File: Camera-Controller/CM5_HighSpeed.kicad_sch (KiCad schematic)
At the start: 19 parts, among them J10 690-019-298-412, J12 USB3_A, J16 Conn_01x22_Female, J22 690-019-298-412, J5 Conn_01x22_Female, J6 THD-02-R, U12 RT9742SNGV, U6 AP22653W6

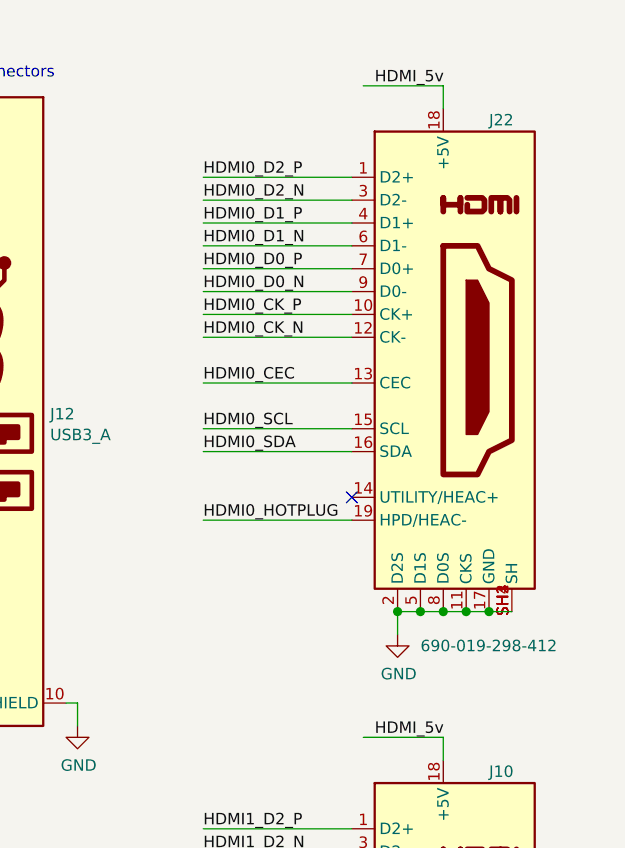
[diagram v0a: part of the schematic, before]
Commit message: Attempted to delete HDMI from sch. #1
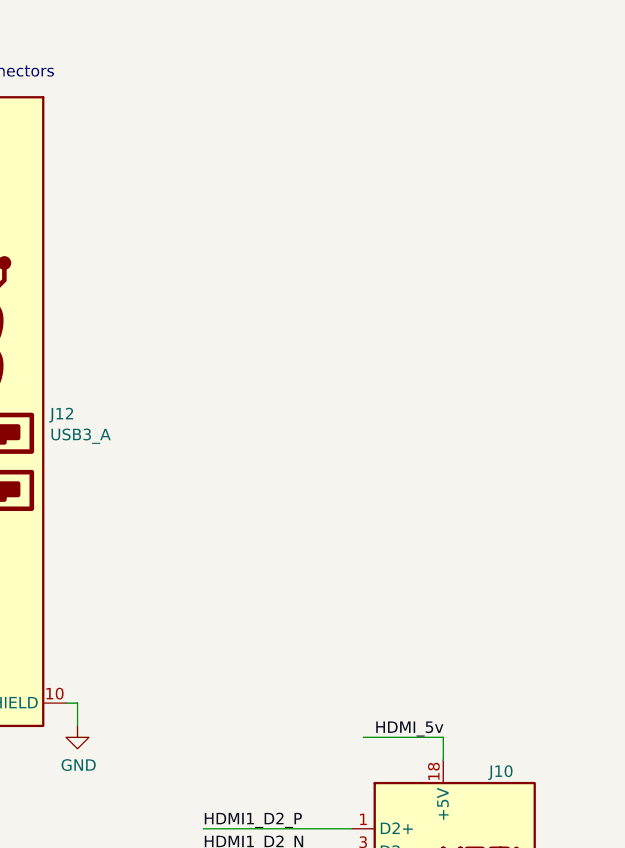
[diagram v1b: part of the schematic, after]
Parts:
- removed J22: 690-019-298-412, CM5IO:EDAC 690-019-298-412, symbol CM5IO:HDMI_A_1.4
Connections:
- no-connect marks 4 -> 3
